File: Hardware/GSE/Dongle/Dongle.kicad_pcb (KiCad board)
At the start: 2 copper layers, 90 x 33 mm, 22 parts, among them J1 USB_A, J2 Conn_Coaxial, J3 Conn_01x02_Male, U1 XBee_SMT, U2 FT231XS, U3 AP2114H-3.3TRG1, U4 TPD3E001DRLR

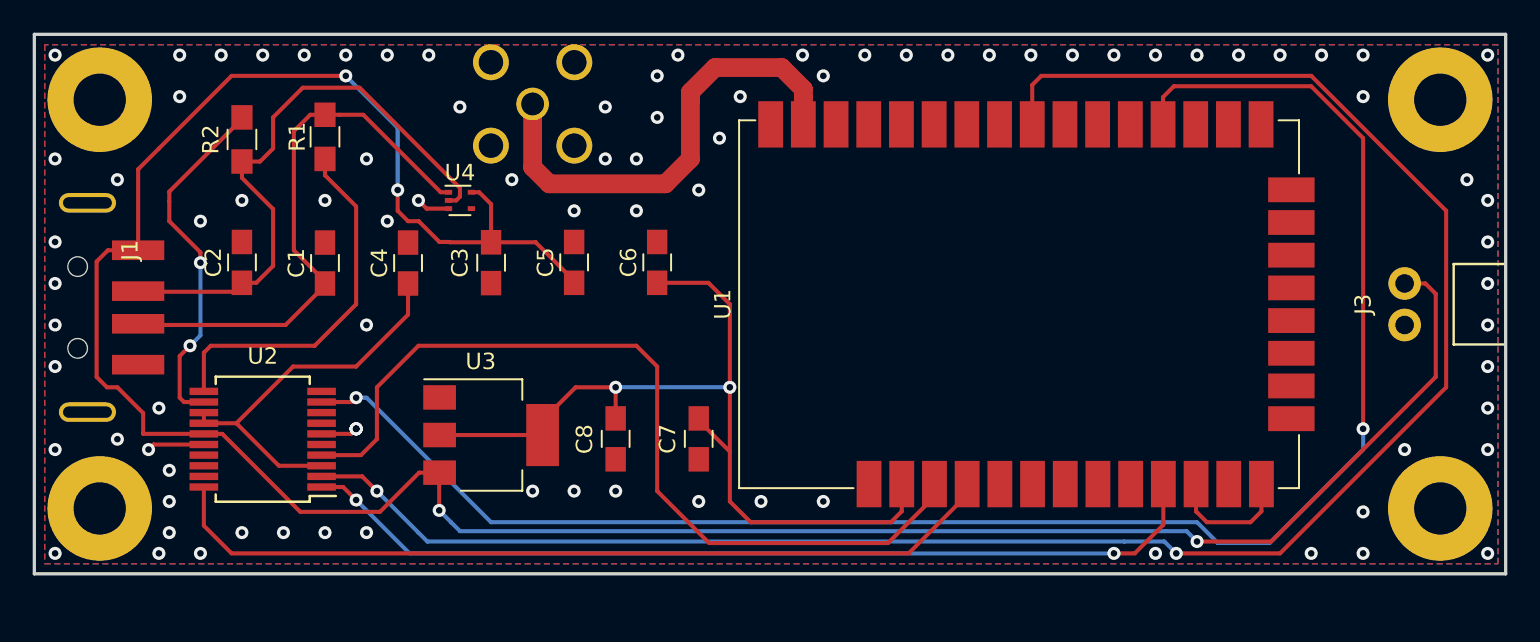
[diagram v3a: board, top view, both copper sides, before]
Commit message: new dongle with LoRa for review
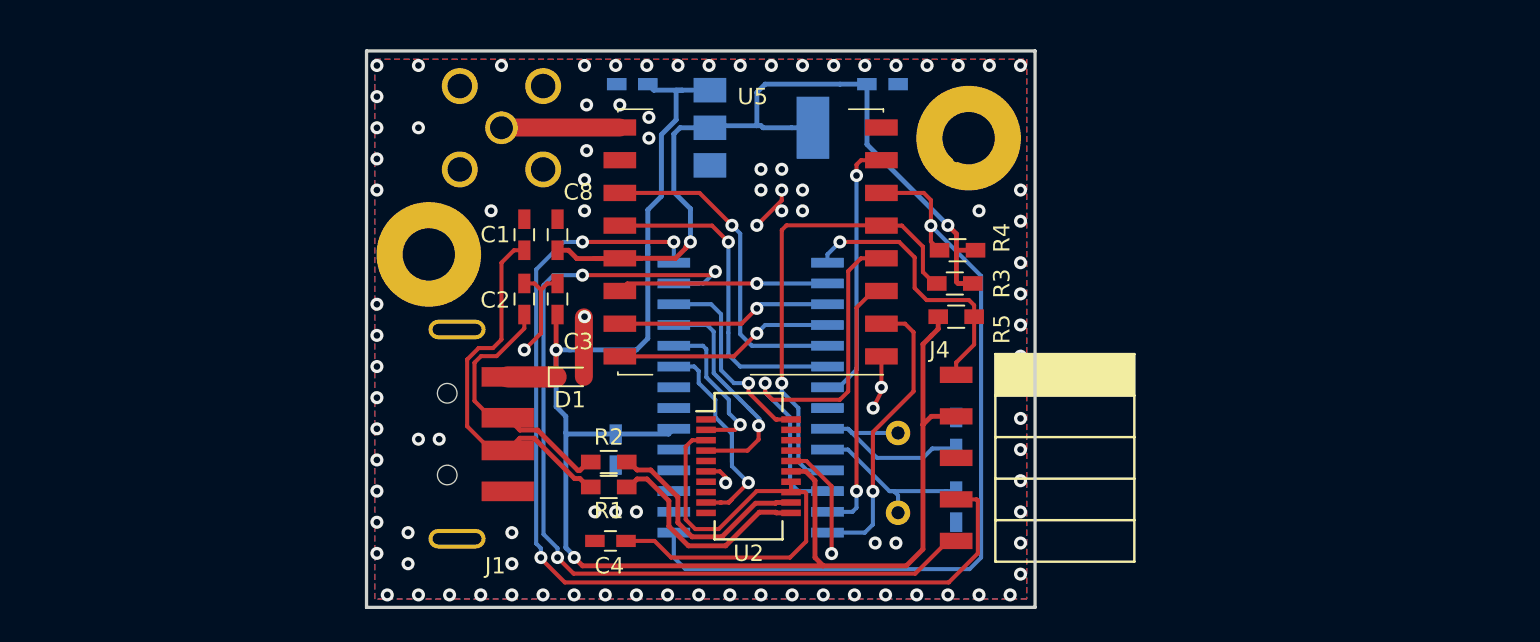
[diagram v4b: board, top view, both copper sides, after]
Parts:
- removed J3: Conn_01x02_Male, Payload2019_Connectors:Molex_KK_1718570002
- removed the REF** at (4.00, 29.0)
- removed the REF** at (4.00, 4.00)
- removed the REF** at (86.0, 29.0)
- removed the REF** at (86.0, 4.00)
- removed U4: TPD3E001DRLR, TO_SOT_Packages_SMD:SOT-553
- added C10: 0.1uF, Capacitors_SMD:C_0603_HandSoldering, B.Cu at (35.6, 25.4)
- added C9: C, Capacitors_SMD:C_0603_HandSoldering, B.Cu at (56.4, 28.9)
- added D1: D_TVS, Diodes_SMD:D_0603, F.Cu at (32.8, 21.0)
- added J4: Conn_01x05_Female, Payload_Connectors:PinHeader_5x2.54_SMD_90deg_952-3198-1-ND, F.Cu at (56.4, 20.8)
- added R3: 10k, Resistors_SMD:R_0603_HandSoldering, F.Cu at (56.4, 17.3)
- added R4: 10k, Resistors_SMD:R_0603_HandSoldering, F.Cu at (56.5, 13.2)
- added R5: 10k, Resistors_SMD:R_0603_HandSoldering, F.Cu at (56.3, 15.2)
- added REF**: MountingHole_3.2mm_M3_Pad, Mounting_Holes:MountingHole_3.2mm_M3_Pad, F.Cu at (57.1, 6.35)
- added REF**: MountingHole_3.2mm_M3_Pad, Mounting_Holes:MountingHole_3.2mm_M3_Pad, F.Cu at (24.1, 13.5)
- added U5: RFM95W-915S2, RF_Modules:Hopref_RFM9XW_SMD, F.Cu at (43.8, 12.7)
- added Y1: Crystal, Crystals:Crystal_HC49-U_Vertical, B.Cu at (52.8, 24.4)
- C1, C2, C3, C4: footprint Capacitors_SMD:C_0805_HandSoldering -> Capacitors_SMD:C_0603_HandSoldering
- C5, C6: footprint Capacitors_SMD:C_0805_HandSoldering -> Capacitors_SMD:C_0603_HandSoldering; moved to B.Cu
- C7: value 100pF -> C; footprint Capacitors_SMD:C_0805_HandSoldering -> Capacitors_SMD:C_0603_HandSoldering; moved to B.Cu
- C8: value 1uF -> 10uF; footprint Capacitors_SMD:C_0805_HandSoldering -> Capacitors_SMD:C_0603_HandSoldering
- J1: footprint Payload2019_Connectors:629104151021 -> Payload_Connectors:629104151021
- J2: footprint Payload2019_Connectors:CONSMA002 -> Payload_Connectors:CONSMA002
- R1, R2: footprint Resistors_SMD:R_0805_HandSoldering -> Resistors_SMD:R_0603_HandSoldering
- U1: value XBee_SMT -> PIC18F26K83; footprint RF_Modules:Digi_XBee_SMT -> Housings_SOIC:SOIC-28W_7.5x18.7mm_Pitch1.27mm; moved to B.Cu
- U2: footprint Housings_SSOP:SSOP-20_5.3x7.2mm_Pitch0.65mm -> Package_SO:SSOP-20_3.9x8.7mm_P0.635mm
- U3: moved to B.Cu
- moved R2 29.9 mm to (35.1, 26.2), turned to 180 degrees
- moved U2 29.8 mm to (43.7, 26.4), turned to 0 degrees
- moved R1 27.6 mm to (35.1, 27.7), turned to 180 degrees
- moved U3 25.0 mm to (44.5, 5.71)
- moved J1 23.9 mm to (29.0, 21.0)
- moved C4 21.0 mm to (35.2, 31.0), turned to 180 degrees
- moved U1 18.1 mm to (43.8, 22.2), turned to 180 degrees
- moved C6 17.6 mm to (51.9, 3.05), turned to 0 degrees
- moved C2 17.4 mm to (30.0, 16.2)
- moved C7 15.8 mm to (56.4, 24.4), turned to 90 degrees
- moved C8 13.0 mm to (32.0, 12.3), turned to 90 degrees
- moved C1 12.3 mm to (30.0, 12.3)
- moved C5 11.5 mm to (36.6, 3.05), turned to 180 degrees
- moved G*** 6.20 mm to (30.9, 23.0)
- moved C3 4.63 mm to (32.0, 16.2), turned to 90 degrees
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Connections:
- net Net-(C1-Pad1) renamed /D1-
- net Net-(C2-Pad1) renamed /D1+
- net Net-(R1-Pad1) renamed /USBD-
- net Net-(R2-Pad1) renamed /USBD+
- C3 pad 1: 5V -> +5V
- C5 pad 1: 5V -> +5V
- C6 pad 1: Net-(C6-Pad1) -> +3V3
- C7 pad 1: Net-(C6-Pad1) -> /OSC1
- C8 pad 1: Net-(C6-Pad1) -> +3V3
- J1 pad 1: 5V -> +5V
- U1 pad 1: GND -> /~MCLR
- U1 pad 10: DTR -> /OSC2
- U1 pad 11: GND -> /CS
- U1 pad 12: Net-(U1-Pad12) -> /SCK
- U1 pad 13: GND -> /MOSI
- U1 pad 14: Net-(U1-Pad14) -> /MISO
- U1 pad 15: Net-(U1-Pad15) -> /RESET
- U1 pad 19: Net-(U1-Pad19) -> GND
- U1 pad 2: Net-(C6-Pad1) -> /DIO0
- U1 pad 20: Net-(U1-Pad20) -> +5V
- U1 pad 22: GND -> Net-(U1-Pad22)
- U1 pad 23: Net-(U1-Pad23) -> /CTS
- U1 pad 24: Net-(U1-Pad24) -> /RTS
- U1 pad 25: CTS -> /DOUT
- U1 pad 26: Net-(U1-Pad26) -> /DIN
- U1 pad 27: Net-(U1-Pad27) -> /ICSPCLK
- U1 pad 28: Net-(U1-Pad28) -> /ICSPDAT
- U1 pad 3: DOUT -> /DIO1
- U1 pad 4: DIN -> /DIO2
- U1 pad 5: Net-(U1-Pad5) -> /DIO3
- U1 pad 6: Net-(U1-Pad6) -> /DIO4
- U1 pad 7: Net-(U1-Pad7) -> /DIO5
- U1 pad 8: Net-(U1-Pad8) -> GND
- U1 pad 9: Net-(U1-Pad9) -> /OSC1
- U2 pad 1: DTR -> Net-(U2-Pad1)
- U2 pad 15: 5V -> +5V
- U2 pad 2: RTS -> /RTS
- U2 pad 20: DIN -> /DIN
- U2 pad 4: DOUT -> /DOUT
- U2 pad 9: CTS -> /CTS
- U3 pad 2: Net-(C6-Pad1) -> +3V3
- U3 pad 3: 5V -> +5V
- U3 pad 4: Net-(C6-Pad1) -> +3V3
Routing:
- net 5V: track 157.6 -> 0.00 mm, vias 4 -> 0
- net RTS: track 117.1 -> 0.00 mm, vias 2 -> 0
- net CTS: track 104.4 -> 0.00 mm, vias 2 -> 0
- net +5V: track 0.00 -> 99.3 mm, vias 0 -> 2
- net /ICSPDAT: track 0.00 -> 60.8 mm, vias 0 -> 3
- net /ICSPCLK: track 0.00 -> 56.8 mm, vias 0 -> 3
- net DTR: track 56.4 -> 0.00 mm, vias 2 -> 0
- net Net-(C6-Pad1): track 54.3 -> 0.00 mm, vias 2 -> 0
- net DOUT: track 53.5 -> 0.00 mm
- net DIN: track 51.9 -> 0.00 mm
- net +3V3: track 0.00 -> 51.8 mm, vias 0 -> 2
- net /RESET: track 0.00 -> 49.0 mm, vias 0 -> 1
- net /CS: track 0.00 -> 28.6 mm, vias 0 -> 1
- net /SCK: track 0.00 -> 25.0 mm, vias 0 -> 1
- net Net-(J2-Pad1): track 28.9 -> 7.25 mm
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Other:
- board size 90 x 33 mm -> 40.9 x 34 mm
- net class 1A trace added: clearance 0.2, trace_width 0.3, via_dia 0.8, via_drill 0.4
- net class RF trace added: clearance 0.2, trace_width 1.1, via_dia 0.8, via_drill 0.4
- net class TVS trace added: clearance 0.2, trace_width 4, via_dia 0.8, via_drill 0.4
- board text added: "BotL V1"
- board text removed: ":partyparrot: rev1 2018"

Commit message: updated dongle based on review
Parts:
- U1: value PIC18F26K83 -> PICLF26K83
- moved C1 3.93 mm to (30.0, 16.2)
- moved C2 3.81 mm to (29.8, 12.4)
- moved R1 1.52 mm to (35.1, 26.2)
- moved R2 1.52 mm to (35.1, 27.7)
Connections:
- C10 pad 2: +5V -> +3V3
- J1 pad 2: /D1+ -> /D1-
- J1 pad 3: /D1- -> /D1+
- R3 pad 1: +5V -> +3V3
- U1 pad 20: +5V -> +3V3
- U2 pad 11: /USBD- -> /USBD+
- U2 pad 12: /USBD+ -> /USBD-
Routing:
- net +3V3: track 51.8 -> 86.7 mm, vias 2 -> 4
- net +5V: track 99.3 -> 85.6 mm
- net /D1-: track 22.8 -> 17.5 mm
- net /D1+: track 17.5 -> 22.8 mm
- net (no net): vias 1 -> 0

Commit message: ARM board refactor
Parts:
- moved R5 0.15 mm to (56.5, 15.2)
- moved C1 0.13 mm to (29.8, 16.2)
- moved R3 0.06 mm to (56.5, 17.3)
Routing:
- net /MOSI: track 16.1 -> 42.0 mm
- net /MISO: track 18.0 -> 35.6 mm
- net GND: track 25.0 -> 19.1 mm, vias 100 -> 106
- net +5V: track 85.6 -> 82.6 mm
- net /RESET: track 49.0 -> 52.0 mm
- net /ICSPDAT: track 60.8 -> 61.7 mm
- net /ICSPCLK: track 56.8 -> 57.5 mm
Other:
- rule pad_to_mask_clearance: 0.2 -> 0
